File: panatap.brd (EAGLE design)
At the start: 47 x 16.5 mm, 23 parts, among them Q1 J310, Q2 BFS17, X1 IF_IN, X2 RF_OUT

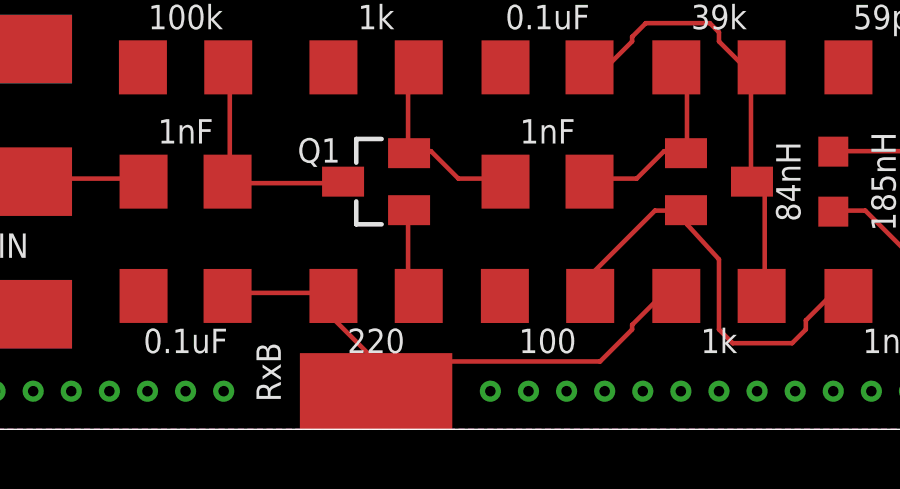
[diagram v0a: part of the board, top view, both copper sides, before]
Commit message: Updated schematic and board with revised capacitor placement
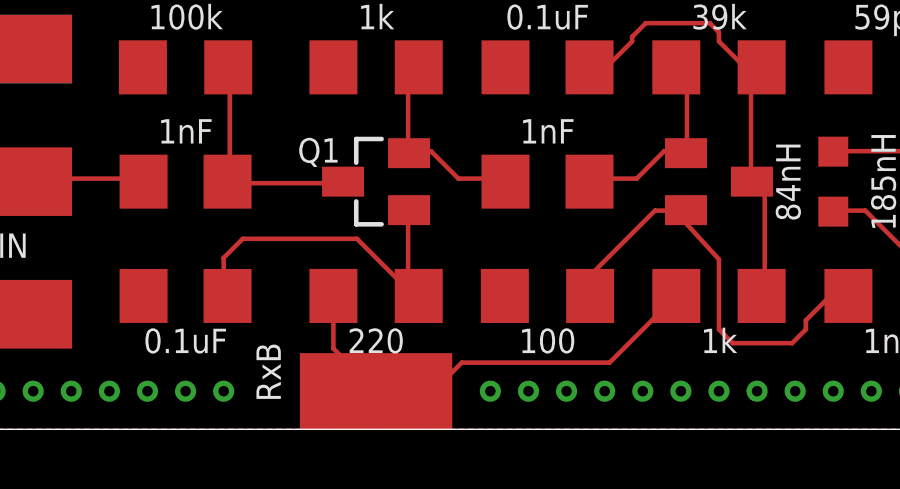
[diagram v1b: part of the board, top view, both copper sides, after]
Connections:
- net N$8: no longer C2.1
- net N$9: now also C2.1
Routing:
- net N$9: track 3.02 -> 11.9 mm
- net N$8: track 19.2 -> 15.1 mm
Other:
- board text added: "rev 0.2 8-30-17"
- board text removed: "rev 0.1"
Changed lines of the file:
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@@
 <setting verticaltext="up"/>
 </settings>
-<grid distance="25" unitdist="mil" unit="mil" style="lines" multiple="1" display="yes" altdistance="5" altunitdist="mil" altunit="mil"/>
+<grid distance="12.5" unitdist="mil" unit="mil" style="lines" multiple="1" display="yes" altdistance="5" altunitdist="mil" altunit="mil"/>
 <layers>
-<layer number="1" name="Top" color="4" fill="1" visible="no" active="yes"/>
+<layer number="1" name="Top" color="4" fill="1" visible="yes" active="yes"/>
 <layer number="2" name="Route2" color="1" fill="3" visible="no" active="no"/>
 <layer number="3" name="Route3" color="4" fill="3" visible="no" active="no"/>
@@
 <text x="38.1" y="16.51" size="1.778" layer="22" font="vector" ratio="15" rot="MR0" align="center-left">W3AXL PanaTap</text>
 <text x="38.1" y="14.605" size="1.016" layer="22" font="vector" ratio="15" rot="MR0" align="center-left">High-impedance IF Panadapter tap</text>
-<text x="38.1" y="13.335" size="1.016" layer="22" font="vector" ratio="15" rot="MR0" align="center-left">rev 0.1</text>
+<text x="38.1" y="13.335" size="1.016" layer="22" font="vector" ratio="15" rot="MR0" align="center-left">rev 0.2 8-30-17</text>
 </plain>
 <attributes>
@@
 </signal>
 <signal name="GNDA">
-<contactref element="C2" pad="2"/>
 <contactref element="C4" pad="2"/>
 <contactref element="R5" pad="2"/>
@@
 <via x="20.32" y="5.715" extent="1-16" drill="0.35"/>
 <via x="19.05" y="5.715" extent="1-16" drill="0.35"/>
+<contactref element="C2" pad="2"/>
 </signal>
 <signal name="N$8">
+<contactref element="R6" pad="1"/>
 <contactref element="R3" pad="2"/>
 <contactref element="PAD1" pad="1"/>
-<contactref element="C2" pad="1"/>
-<contactref element="R6" pad="1"/>
-<wire x1="13.716" y1="8.9916" x2="10.3632" y2="8.9916" width="0.1524" layer="1"/>
-<wire x1="10.3632" y1="8.9916" x2="10.29" y2="8.89" width="0.1524" layer="1"/>
-<wire x1="13.716" y1="8.9916" x2="13.818" y2="8.89" width="0.1524" layer="1"/>
-<wire x1="24.6888" y1="8.8392" x2="25.146" y2="8.8392" width="0.1524" layer="1"/>
-<wire x1="23.7744" y1="7.9248" x2="24.6888" y2="8.8392" width="0.1524" layer="1"/>
-<wire x1="23.7744" y1="7.7724" x2="23.7744" y2="7.9248" width="0.1524" layer="1"/>
-<wire x1="22.7076" y1="6.7056" x2="23.7744" y2="7.7724" width="0.1524" layer="1"/>
-<wire x1="16.1544" y1="6.7056" x2="22.7076" y2="6.7056" width="0.1524" layer="1"/>
-<wire x1="15.24" y1="5.7912" x2="15.6972" y2="6.2484" width="0.1524" layer="1"/>
-<wire x1="15.6972" y1="6.2484" x2="16.1544" y2="6.7056" width="0.1524" layer="1"/>
-<wire x1="25.146" y1="8.8392" x2="25.248" y2="8.89" width="0.1524" layer="1"/>
-<wire x1="15.24" y1="5.7912" x2="15.24" y2="5.715" width="0.1524" layer="1"/>
-<wire x1="13.8684" y1="8.0772" x2="13.8684" y2="8.8392" width="0.1524" layer="1"/>
-<wire x1="15.6972" y1="6.2484" x2="13.8684" y2="8.0772" width="0.1524" layer="1"/>
-<wire x1="13.8684" y1="8.8392" x2="13.818" y2="8.89" width="0.1524" layer="1"/>
-<wire x1="15.6972" y1="6.2484" x2="15.24" y2="5.715" width="0.1524" layer="1"/>
+<wire x1="13.818" y1="8.89" x2="13.818" y2="7.137" width="0.1524" layer="1"/>
+<wire x1="13.818" y1="7.137" x2="15.24" y2="5.715" width="0.1524" layer="1"/>
+<wire x1="15.24" y1="5.715" x2="17.145" y2="5.715" width="0.1524" layer="1"/>
+<wire x1="18.0975" y1="6.6675" x2="23.0255" y2="6.6675" width="0.1524" layer="1"/>
+<wire x1="23.0255" y1="6.6675" x2="25.248" y2="8.89" width="0.1524" layer="1"/>
+<wire x1="17.145" y1="5.715" x2="18.0975" y2="6.6675" width="0.1524" layer="1"/>
 </signal>
 <signal name="N$9">
@@
 <wire x1="16.3068" y1="11.7348" x2="16.34" y2="11.75" width="0.1524" layer="1"/>
 <wire x1="16.6116" y1="8.9916" x2="16.662" y2="8.89" width="0.1524" layer="1"/>
+<contactref element="C2" pad="1"/>
+<wire x1="16.662" y1="8.89" x2="16.51" y2="8.89" width="0.1524" layer="1"/>
+<wire x1="16.51" y1="8.89" x2="14.605" y2="10.795" width="0.1524" layer="1"/>
+<wire x1="14.605" y1="10.795" x2="10.795" y2="10.795" width="0.1524" layer="1"/>
+<wire x1="10.795" y1="10.795" x2="10.16" y2="10.16" width="0.1524" layer="1"/>
+<wire x1="10.16" y1="10.16" x2="10.16" y2="9.02" width="0.1524" layer="1"/>
+<wire x1="10.16" y1="9.02" x2="10.29" y2="8.89" width="0.1524" layer="1"/>
 </signal>
 <signal name="N$10">

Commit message: filter values changed, LTSpice added
filter values changed to real, obtainable components and added LTSpice simulation file
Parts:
- C6, C8: value 59pF -> 56pF
- C7: value 69F -> 68pF
- L1, L4: value 84nH -> 82nH
- L2, L3: value 185nH -> 180nH
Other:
- board text added: "180nH"
- board text added: "56pF"
- board text added: "68pF"
- board text added: "82nH"
- board text removed: "185nH"
- board text removed: "59pF"
- board text removed: "69nF"
- board text removed: "84nH"
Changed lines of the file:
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@@
 <text x="26.67" y="6.985" size="0.8128" layer="21" font="vector" ratio="15" align="bottom-center">1k</text>
 <text x="26.67" y="17.78" size="0.8128" layer="21" font="vector" ratio="15" align="bottom-center">39k</text>
-<text x="32.385" y="17.78" size="0.8128" layer="21" font="vector" ratio="15" align="bottom-center">59pF</text>
-<text x="38.1" y="17.78" size="0.8128" layer="21" font="vector" ratio="15" align="bottom-center">59pF</text>
-<text x="38.1" y="6.985" size="0.8128" layer="21" font="vector" ratio="15" align="bottom-center">69nF</text>
-<text x="28.575" y="12.7" size="0.8128" layer="21" font="vector" ratio="15" rot="R270" align="bottom-center">84nH</text>
-<text x="31.75" y="12.7" size="0.8128" layer="21" font="vector" ratio="15" rot="R270" align="bottom-center">185nH</text>
-<text x="34.925" y="12.7" size="0.8128" layer="21" font="vector" ratio="15" rot="R270" align="bottom-center">185nH</text>
-<text x="38.1" y="12.7" size="0.8128" layer="21" font="vector" ratio="15" rot="R270" align="bottom-center">84nH</text>
+<text x="32.385" y="17.78" size="0.8128" layer="21" font="vector" ratio="15" align="bottom-center">56pF</text>
+<text x="38.1" y="17.78" size="0.8128" layer="21" font="vector" ratio="15" align="bottom-center">56pF</text>
+<text x="38.1" y="6.985" size="0.8128" layer="21" font="vector" ratio="15" align="bottom-center">68pF</text>
+<text x="28.575" y="12.7" size="0.8128" layer="21" font="vector" ratio="15" rot="R270" align="bottom-center">82nH</text>
+<text x="31.75" y="12.7" size="0.8128" layer="21" font="vector" ratio="15" rot="R270" align="bottom-center">180nH</text>
+<text x="34.925" y="12.7" size="0.8128" layer="21" font="vector" ratio="15" rot="R270" align="bottom-center">180nH</text>
+<text x="38.1" y="12.7" size="0.8128" layer="21" font="vector" ratio="15" rot="R270" align="bottom-center">82nH</text>
 <text x="44.45" y="10.16" size="0.8128" layer="21" font="vector" ratio="15" align="bottom-center">RF OUT</text>
 <text x="2.54" y="10.16" size="0.8128" layer="21" font="vector" ratio="15" align="bottom-center">IF IN</text>
@@
 <element name="C4" library="resistor" library_urn="urn:adsk.eagle:library:348" package="C1206" value="0.1uF" x="20.955" y="16.51" smashed="yes" rot="R180"/>
 <element name="C5" library="resistor" library_urn="urn:adsk.eagle:library:348" package="C1206" value="1nF" x="32.385" y="8.89" smashed="yes"/>
-<element name="C6" library="resistor" library_urn="urn:adsk.eagle:library:348" package="C1206" value="59pF" x="32.385" y="16.51" smashed="yes" rot="R180"/>
-<element name="C7" library="resistor" library_urn="urn:adsk.eagle:library:348" package="C1206" value="69F" x="38.1" y="8.89" smashed="yes" rot="R180"/>
-<element name="C8" library="resistor" library_urn="urn:adsk.eagle:library:348" package="C1206" value="59pF" x="38.1" y="16.51" smashed="yes" rot="R180"/>
-<element name="L1" library="resistor" library_urn="urn:adsk.eagle:library:348" package="L2012C" value="84nH" x="30.48" y="12.7" smashed="yes" rot="R90"/>
-<element name="L2" library="resistor" library_urn="urn:adsk.eagle:library:348" package="L2012C" value="185nH" x="33.655" y="12.7" smashed="yes" rot="R270"/>
-<element name="L3" library="resistor" library_urn="urn:adsk.eagle:library:348" package="L2012C" value="185nH" x="36.83" y="12.7" smashed="yes" rot="R90"/>
-<element name="L4" library="resistor" library_urn="urn:adsk.eagle:library:348" package="L2012C" value="84nH" x="40.005" y="12.7" smashed="yes" rot="R270"/>
+<element name="C6" library="resistor" library_urn="urn:adsk.eagle:library:348" package="C1206" value="56pF" x="32.385" y="16.51" smashed="yes" rot="R180"/>
+<element name="C7" library="resistor" library_urn="urn:adsk.eagle:library:348" package="C1206" value="68pF" x="38.1" y="8.89" smashed="yes" rot="R180"/>
+<element name="C8" library="resistor" library_urn="urn:adsk.eagle:library:348" package="C1206" value="56pF" x="38.1" y="16.51" smashed="yes" rot="R180"/>
+<element name="L1" library="resistor" library_urn="urn:adsk.eagle:library:348" package="L2012C" value="82nH" x="30.48" y="12.7" smashed="yes" rot="R90"/>
+<element name="L2" library="resistor" library_urn="urn:adsk.eagle:library:348" package="L2012C" value="180nH" x="33.655" y="12.7" smashed="yes" rot="R270"/>
+<element name="L3" library="resistor" library_urn="urn:adsk.eagle:library:348" package="L2012C" value="180nH" x="36.83" y="12.7" smashed="yes" rot="R90"/>
+<element name="L4" library="resistor" library_urn="urn:adsk.eagle:library:348" package="L2012C" value="82nH" x="40.005" y="12.7" smashed="yes" rot="R270"/>
 <element name="PAD1" library="wirepad" library_urn="urn:adsk.eagle:library:412" package="SMD2,54-5,08" value="VCC" x="15.24" y="5.715" smashed="yes" rot="R270">
 <attribute name="VALUE" x="15.24" y="5.715" size="0.0254" layer="27" rot="R270"/>
